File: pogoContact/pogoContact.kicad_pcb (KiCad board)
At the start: 2 copper layers, 36.9 x 41 mm, 6 parts, among them J1 Conn_01x06, J2 Conn_01x03, J3 Conn_01x03

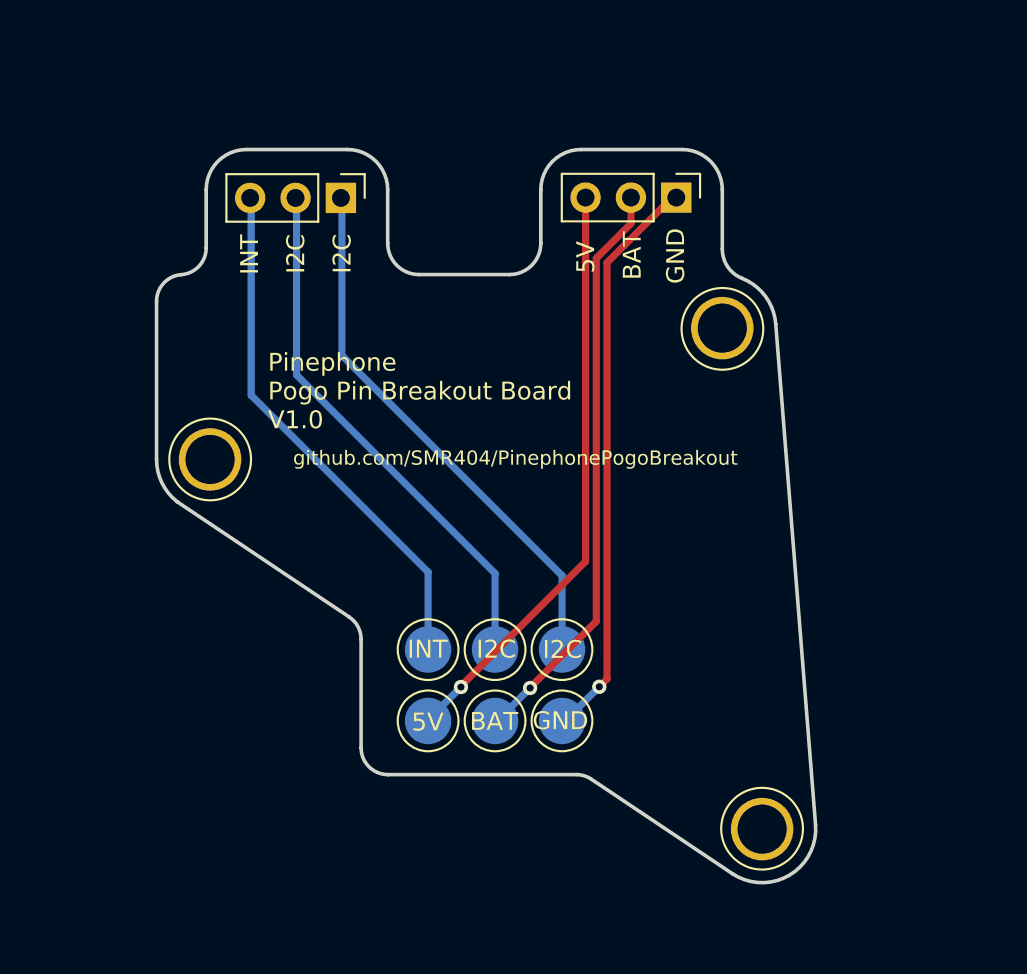
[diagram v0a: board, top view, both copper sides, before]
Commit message: Updated pogo breakout board silkscreen, switched front to ground fill and widened power traces
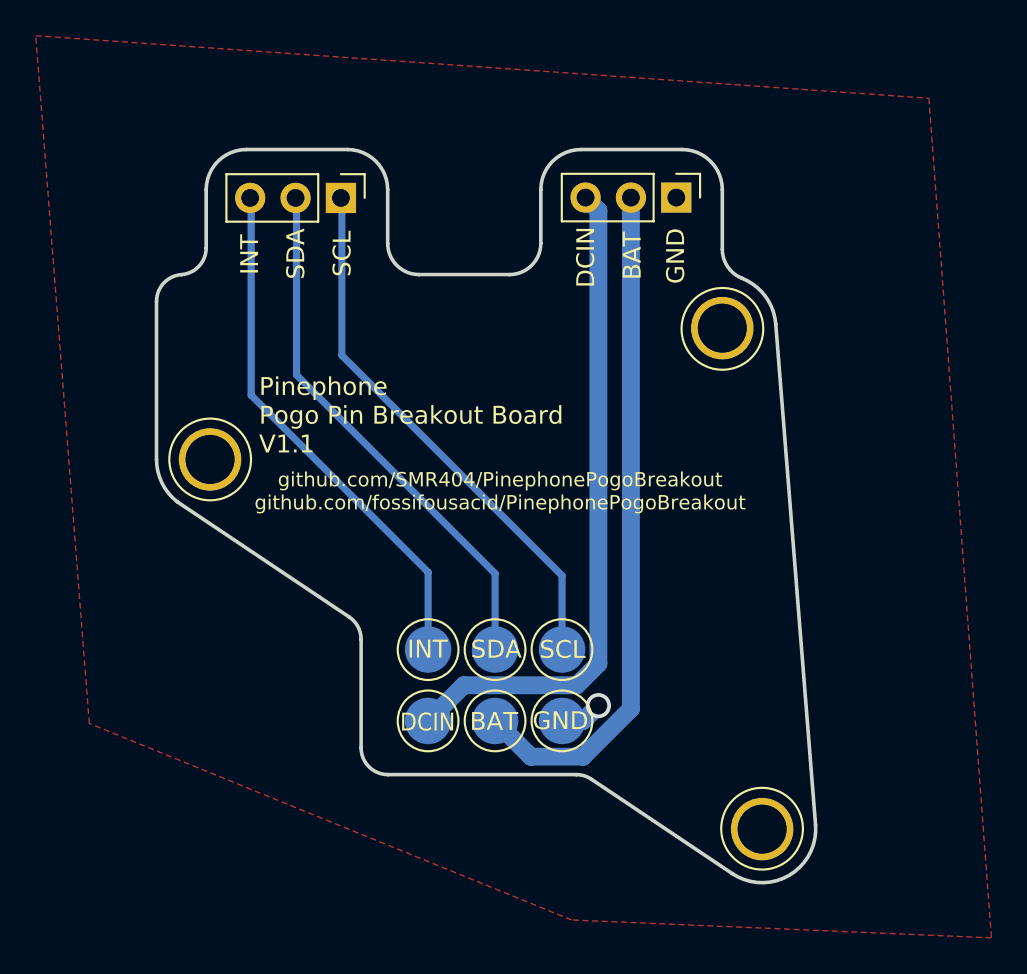
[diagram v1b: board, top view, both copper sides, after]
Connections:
- net Net-(J1-Pad1) renamed /SCL
- net Net-(J1-Pad2) renamed /SDA
- net Net-(J1-Pad3) renamed /INT
- net Net-(J1-Pad4) renamed /GND
- net Net-(J1-Pad5) renamed /BAT
- net Net-(J1-Pad6) renamed /DCIN
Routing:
- net /GND: track 32.2 -> 2.39 mm
- net /BAT: track 32.7 -> 38.2 mm, vias 1 -> 0
- net /DCIN: track 33.3 -> 37.3 mm, vias 1 -> 0
- net /SCL: track 31.0 -> 30.3 mm
- added copper zone on F.Cu, net /GND
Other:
- net class Default removed
- board text added: "DCIN"
- board text added: "Pinephone Pogo Pin Breakout Board V1.1"
- board text added: "SCL"
- board text added: "SDA"
- board text added: "github.com/SMR404/PinephonePogoBreakout github.com/fossifousacid/PinephonePogoBreakout"
- board text removed: "5V"
- board text removed: "I2C"
- board text removed: "Pinephone Pogo Pin Breakout Board V1.0"
- board text removed: "github.com/SMR404/PinephonePogoBreakout"
